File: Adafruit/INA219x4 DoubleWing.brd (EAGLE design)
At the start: 50.8 x 47 mm, 42 parts, among them J1 3.5mm, J2 3.5mm, J3 3.5mm, J4 3.5mm, U1 INA219BIDCNT, U2 INA219BIDCNT, U3 INA219BIDCNT, U4 INA219BIDCNT

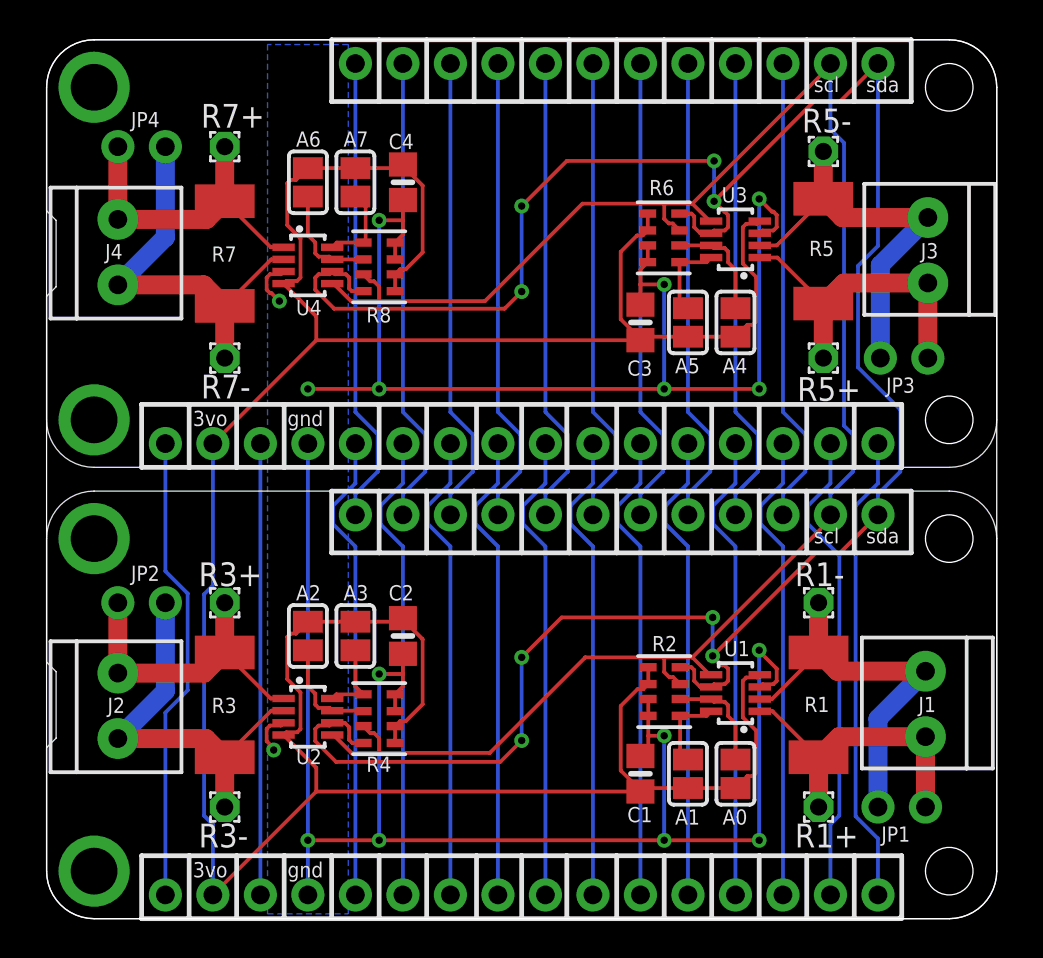
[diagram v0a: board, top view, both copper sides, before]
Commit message: Renaming "INA219x4 FeatherWing" to "INA219x4 DoubleWing"
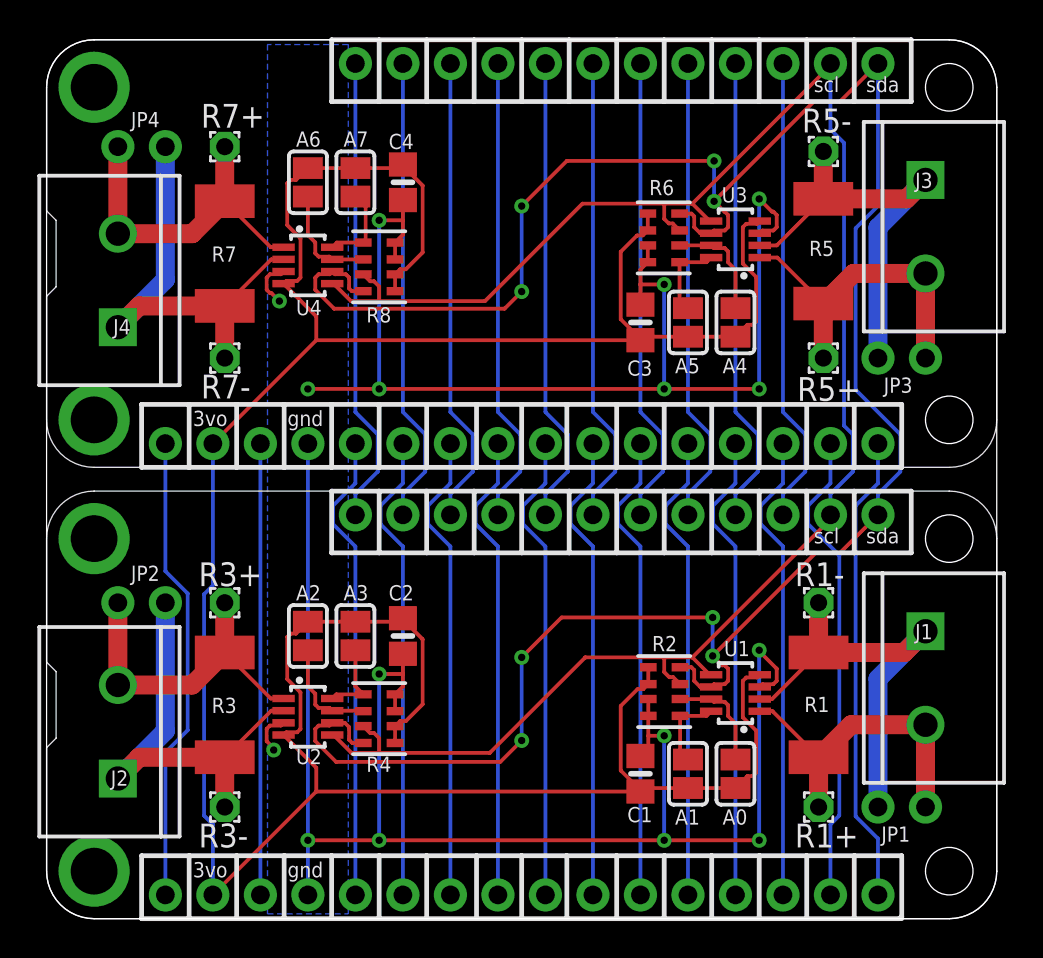
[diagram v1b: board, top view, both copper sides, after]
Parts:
- J1, J2, J3, J4: value 3.5mm -> 5mm; device microbuilder:TERMBLOCK_1X2-3.5MM -> SparkFun-Connectors:SCREWTERMINAL-5MM-2
- moved J4 4.06 mm to (3.81, 31.6), turned to 90 degrees
- moved J1 3.94 mm to (47.0, 15.4), turned to 270 degrees
- moved J2 3.94 mm to (3.81, 7.49), turned to 90 degrees
- moved J3 3.81 mm to (47.0, 39.5), turned to 270 degrees
- moved JP3 0.13 mm to (45.7, 30.0)
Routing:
- net VIN4-: track 21.6 -> 23.9 mm
- net VIN2-: track 21.3 -> 23.5 mm
- net VIN1-: track 21.3 -> 23.5 mm
- net VIN3-: track 21.5 -> 23.4 mm
- net VIN4+: track 17.1 -> 18.2 mm
- net VIN1+: track 16.8 -> 17.7 mm
- net VIN2+: track 16.8 -> 17.7 mm
- net VIN3+: track 17.4 -> 18.0 mm
